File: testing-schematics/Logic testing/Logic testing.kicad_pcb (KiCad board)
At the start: 2 copper layers, 38 parts, among them J4 Lame Tab, K1 G6K-2, K2 G6K-2, K3 G6K-2, K4 G6K-2, K5 G6K-2, P1 USB_C_Plug_USB2.0, Q1 BC547, Q2 BC547, Q3 BC547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

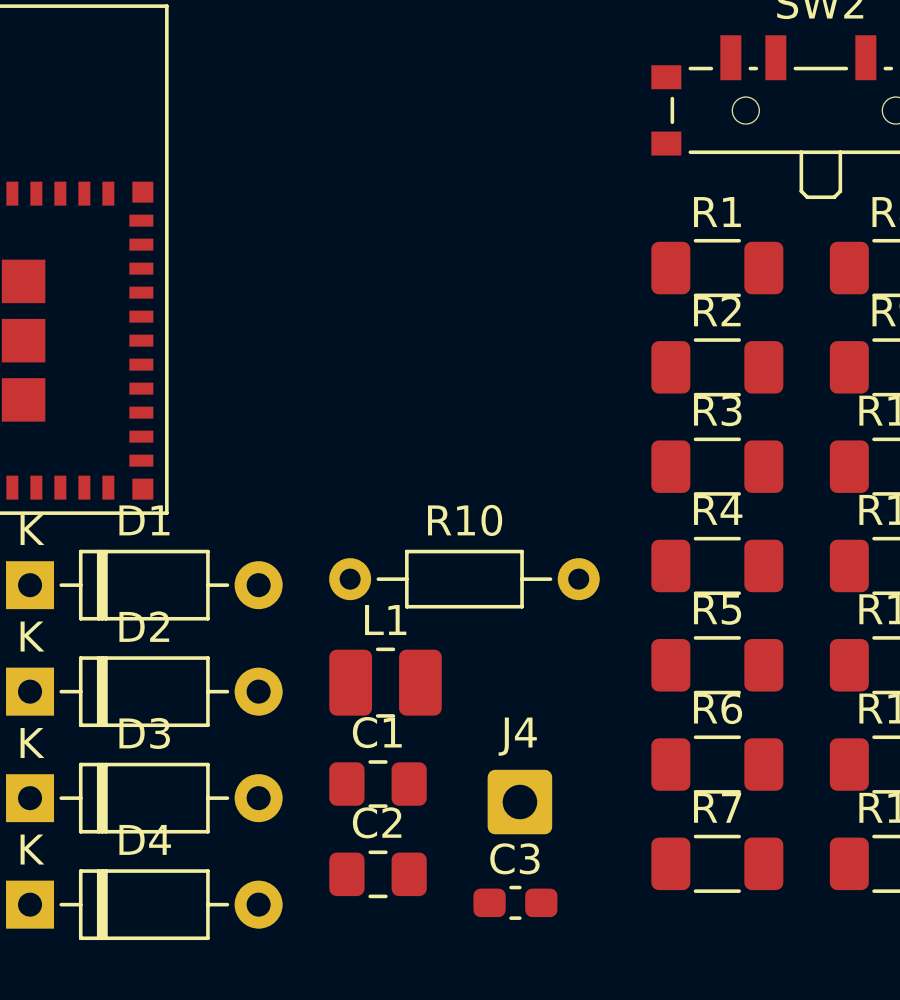
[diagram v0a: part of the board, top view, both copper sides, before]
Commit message: Journal; BOM changes; PCB changes
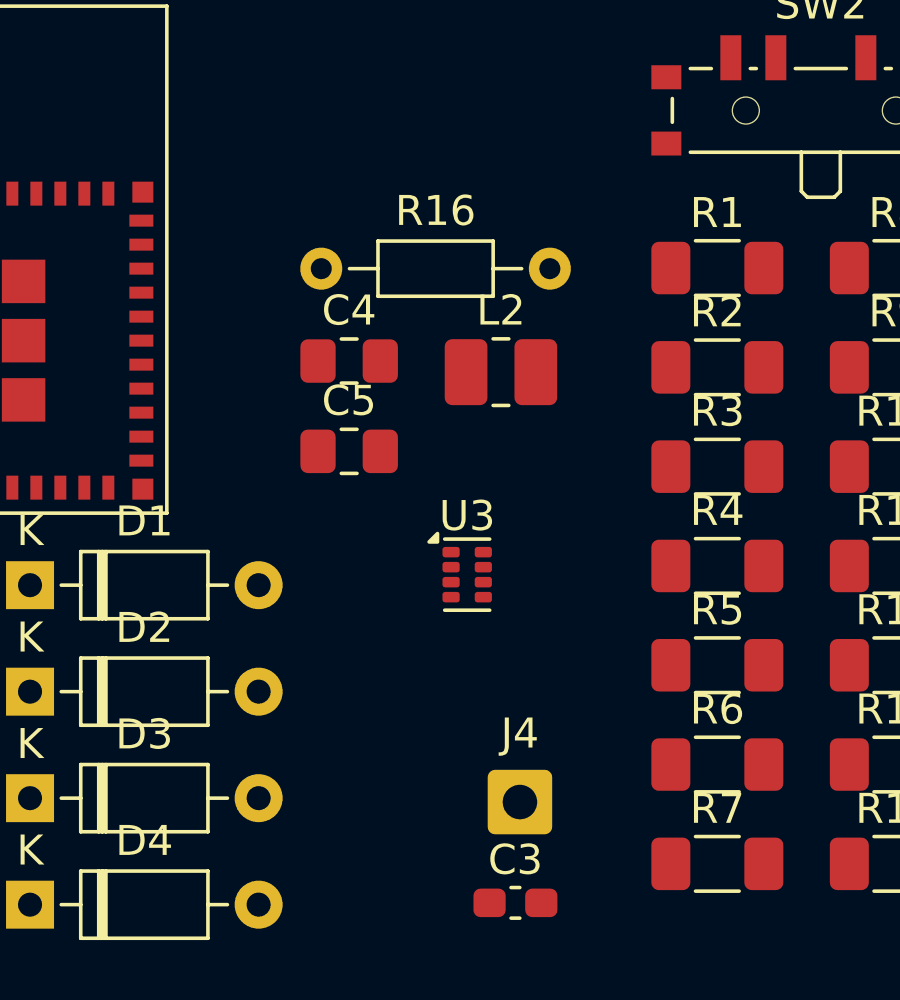
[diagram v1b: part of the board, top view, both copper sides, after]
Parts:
- removed C1: 4.7 µF, Capacitor_SMD:C_0805_2012Metric_Pad1.18x1.45mm_HandSolder
- removed C2: 10 µF, Capacitor_SMD:C_0805_2012Metric_Pad1.18x1.45mm_HandSolder
- removed L1: 2.2 µH, Inductor_SMD:L_1008_2520Metric_Pad1.43x2.20mm_HandSolder
- removed R10: 267k, Resistor_THT:R_Axial_DIN0204_L3.6mm_D1.6mm_P7.62mm_Horizontal
- added C4: 10 µF, Capacitor_SMD:C_0805_2012Metric_Pad1.18x1.45mm_HandSolder, F.Cu at (173.0, 86.1)
- added C5: 4.7 µF, Capacitor_SMD:C_0805_2012Metric_Pad1.18x1.45mm_HandSolder, F.Cu at (173.0, 89.1)
- added L2: 2.2 µH, Inductor_SMD:L_1008_2520Metric_Pad1.43x2.20mm_HandSolder, F.Cu at (178.1, 86.5)
- added R16: 267k, Resistor_THT:R_Axial_DIN0204_L3.6mm_D1.6mm_P7.62mm_Horizontal, F.Cu at (172.1, 83.0)
- added U3: TPS62840DLCR, Package_SON:VSON-8_1.5x2mm_P0.5mm, F.Cu at (177.0, 93.2)
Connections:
- net REG_GND renamed VD1

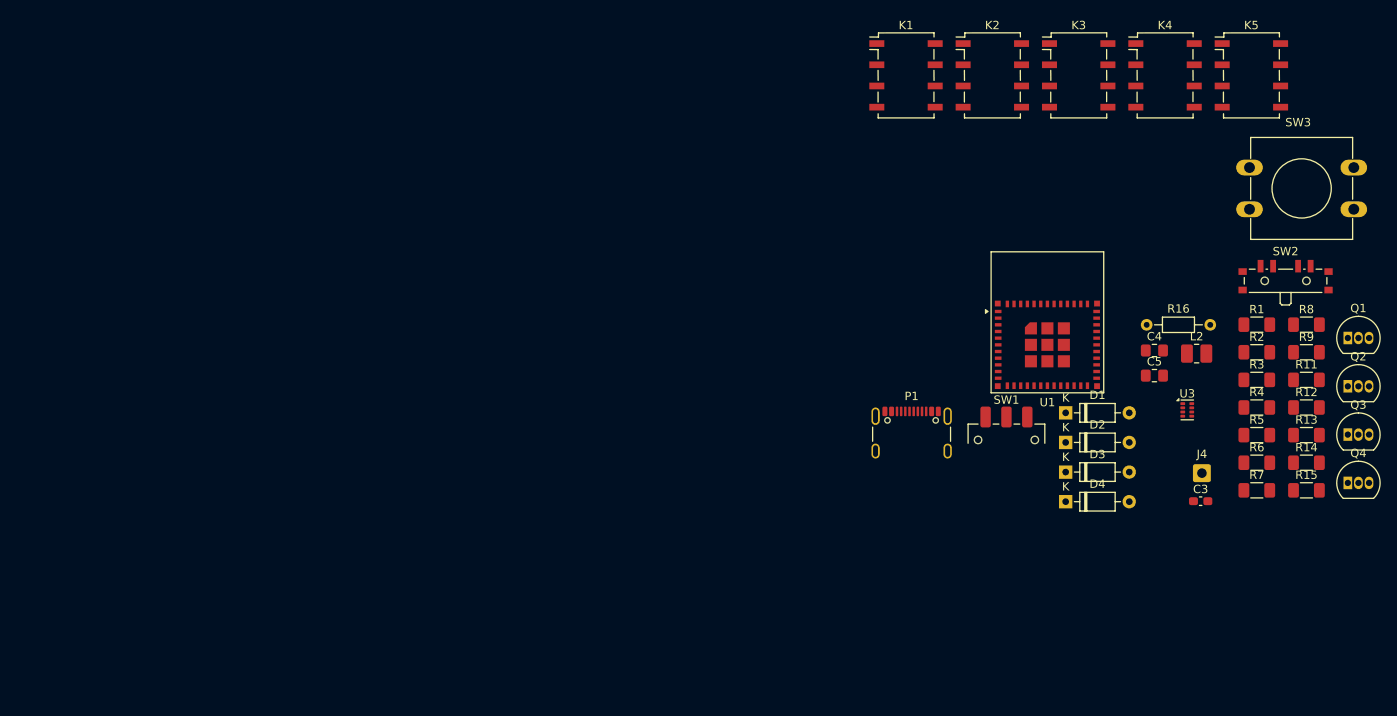
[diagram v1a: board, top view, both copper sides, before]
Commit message: Worked on new power; Worked on display; Replaces ESP controller; Restructured schematic; Worked on PCB layout; Did journal
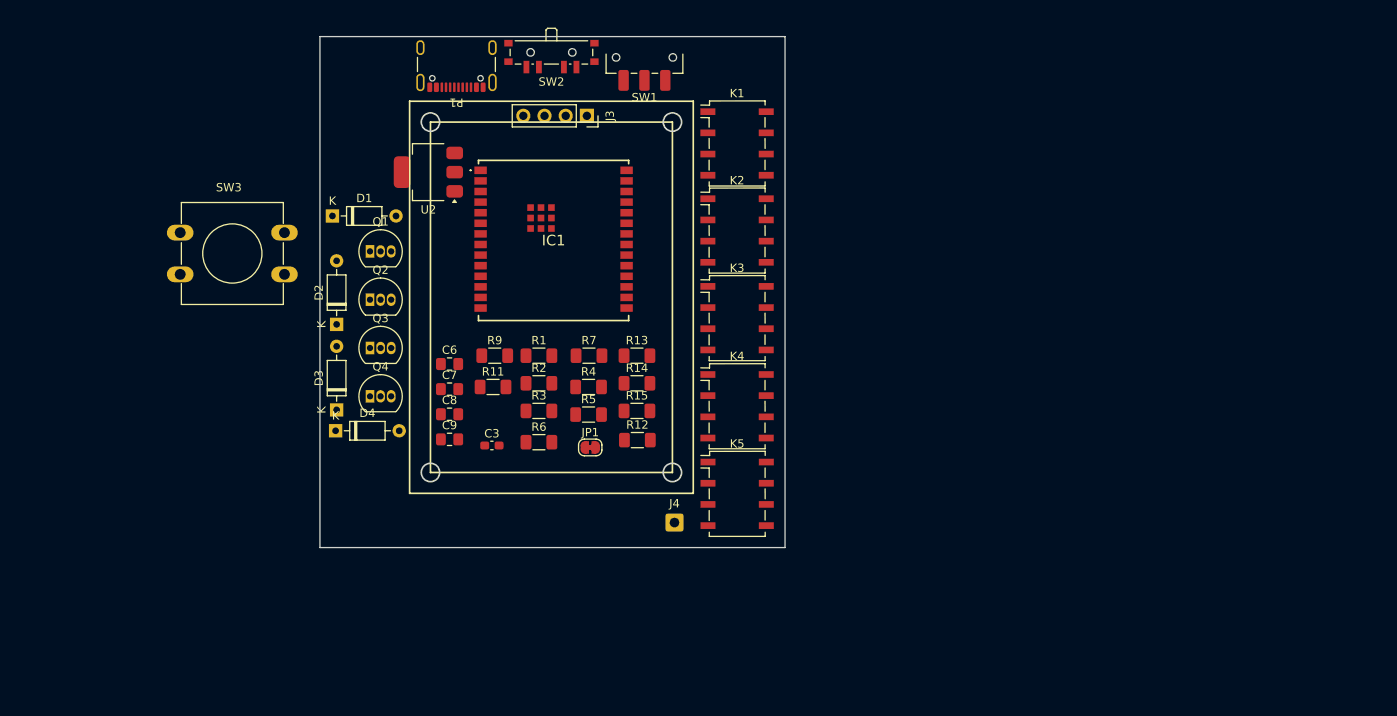
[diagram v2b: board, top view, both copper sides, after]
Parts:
- removed C4: 10 µF, Capacitor_SMD:C_0805_2012Metric_Pad1.18x1.45mm_HandSolder
- removed C5: 4.7 µF, Capacitor_SMD:C_0805_2012Metric_Pad1.18x1.45mm_HandSolder
- removed L2: 2.2 µH, Inductor_SMD:L_1008_2520Metric_Pad1.43x2.20mm_HandSolder
- removed R16: 267k, Resistor_THT:R_Axial_DIN0204_L3.6mm_D1.6mm_P7.62mm_Horizontal
- removed R8: 0Ω, Resistor_SMD:R_1206_3216Metric_Pad1.30x1.75mm_HandSolder
- removed U1: ESP32-C6-MINI-1, RF_Module:ESP32-C6-MINI-1
- removed U3: TPS62840DLCR, Package_SON:VSON-8_1.5x2mm_P0.5mm
- added C6: 10 µF, Capacitor_SMD:C_0805_2012Metric_Pad1.18x1.45mm_HandSolder, F.Cu at (88.5, 87.8)
- added C7: 10 µF, Capacitor_SMD:C_0805_2012Metric_Pad1.18x1.45mm_HandSolder, F.Cu at (88.5, 90.8)
- added C8: 0.1 µF, Capacitor_SMD:C_0805_2012Metric_Pad1.18x1.45mm_HandSolder, F.Cu at (88.5, 93.8)
- added C9: 0.1 µF, Capacitor_SMD:C_0805_2012Metric_Pad1.18x1.45mm_HandSolder, F.Cu at (88.5, 96.8)
- added IC1: ESP32-C6-WROOM-1U-N8, Importer:ESP32C6WROOM1UN8, F.Cu at (101.0, 72.9)
- added J3: Conn_01x04, Connector_PinSocket_2.54mm:PinSocket_1x04_P2.54mm_Vertical, F.Cu at (105.0, 58.0)
- added JP1: SolderJumper_2_Closed, Jumper:SolderJumper-2_P1.3mm_Bridged_RoundedPad1.0x1.5mm, F.Cu at (105.4, 97.8)
- added U2: AMS1117-3.3, Package_TO_SOT_SMD:SOT-223, F.Cu at (86.0, 64.8)
- moved SW3 128.4 mm to (56.2, 72.0)
- moved Q1 117.7 mm to (79.0, 74.2)
- moved Q2 117.7 mm to (79.0, 80.0)
- moved Q3 117.7 mm to (79.0, 85.8)
- moved Q4 117.7 mm to (79.0, 91.6)
- moved R11 97.5 mm to (93.8, 90.5)
- moved R9 97.3 mm to (94.0, 86.8)
- moved SW2 92.0 mm to (100.8, 50.7), turned to 180 degrees
- moved D1 91.0 mm to (74.5, 70.0)
- moved D2 88.5 mm to (75.0, 83.0), turned to 90 degrees
- moved D4 87.9 mm to (74.9, 95.8)
- moved D3 87.7 mm to (75.0, 93.2), turned to 90 degrees
- moved R1 86.1 mm to (99.2, 86.8)
- moved R2 86.1 mm to (99.2, 90.1)
- moved R3 86.1 mm to (99.2, 93.4)
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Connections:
- SW1 pad 2: Net-(SW1-B) -> EN
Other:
- board outline added: 55.8 x 61.2 mm

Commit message: Worked on connectors, PCB layout, created footprints, component CAD, journal
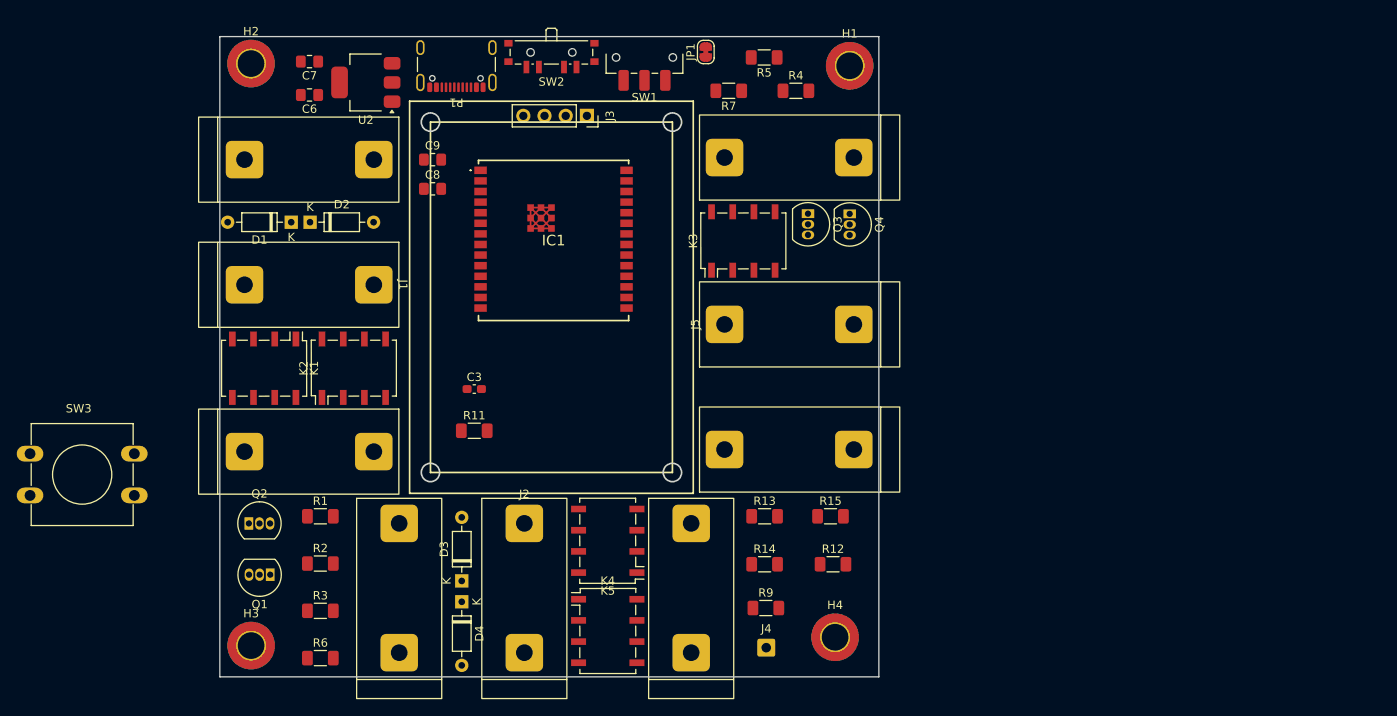
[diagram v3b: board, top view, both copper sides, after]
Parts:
- added H1: MountingHole, MountingHole:MountingHole_3.2mm_M3_ISO7380_Pad_TopBottom, F.Cu at (136.5, 52.0)
- added H2: MountingHole, MountingHole:MountingHole_3.2mm_M3_ISO7380_Pad_TopBottom, F.Cu at (64.7, 51.7)
- added H3: MountingHole, MountingHole:MountingHole_3.2mm_M3_ISO7380_Pad_TopBottom, F.Cu at (64.8, 121.5)
- added H4: MountingHole, MountingHole:MountingHole_3.2mm_M3_ISO7380_Pad_TopBottom, F.Cu at (134.8, 120.5)
- added J1: External Box, Custom:Fencing Plug, F.Cu at (82.5, 78.2)
- added J2: Aux Wire, Custom:Fencing Plug, F.Cu at (97.5, 103.8)
- added J5: Test Output, Custom:Fencing Plug, F.Cu at (118.5, 83.0)
- moved K1 62.8 mm to (66.3, 88.2), turned to -90 degrees
- moved Q4 61.5 mm to (136.5, 69.8), turned to -90 degrees
- moved Q3 54.9 mm to (131.5, 69.7), turned to -90 degrees
- moved JP1 49.4 mm to (119.2, 50.4), turned to 90 degrees
- moved K2 48.8 mm to (77.1, 88.2), turned to 90 degrees
- moved R5 47.7 mm to (126.2, 51.0), turned to 180 degrees
- moved R9 44.4 mm to (126.5, 117.0)
- moved R4 43.3 mm to (130.1, 55.0)
- moved C7 42.7 mm to (71.8, 51.5), turned to 180 degrees
- moved Q1 40.6 mm to (67.0, 113.0), turned to 180 degrees
- moved R6 36.8 mm to (73.0, 123.0)
- moved C6 36.4 mm to (71.8, 55.5), turned to 180 degrees
- moved R7 35.9 mm to (122.0, 55.0), turned to 180 degrees
- moved R3 35.5 mm to (73.0, 117.3)
- moved R2 34.0 mm to (73.0, 111.7)
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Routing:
- net VD1: track 0.00 -> 21.6 mm
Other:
- board size 55.8 x 61.2 mm -> 79 x 76.8 mm
